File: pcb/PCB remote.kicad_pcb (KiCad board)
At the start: 2 copper layers, 58 x 84.9 mm, 11 parts, among them J1 Conn_01x01, J2 Conn_01x01, SW1 GREEN, SW2 RED, U1 RFM69HW, U2 SSD1306, U3 Joystick

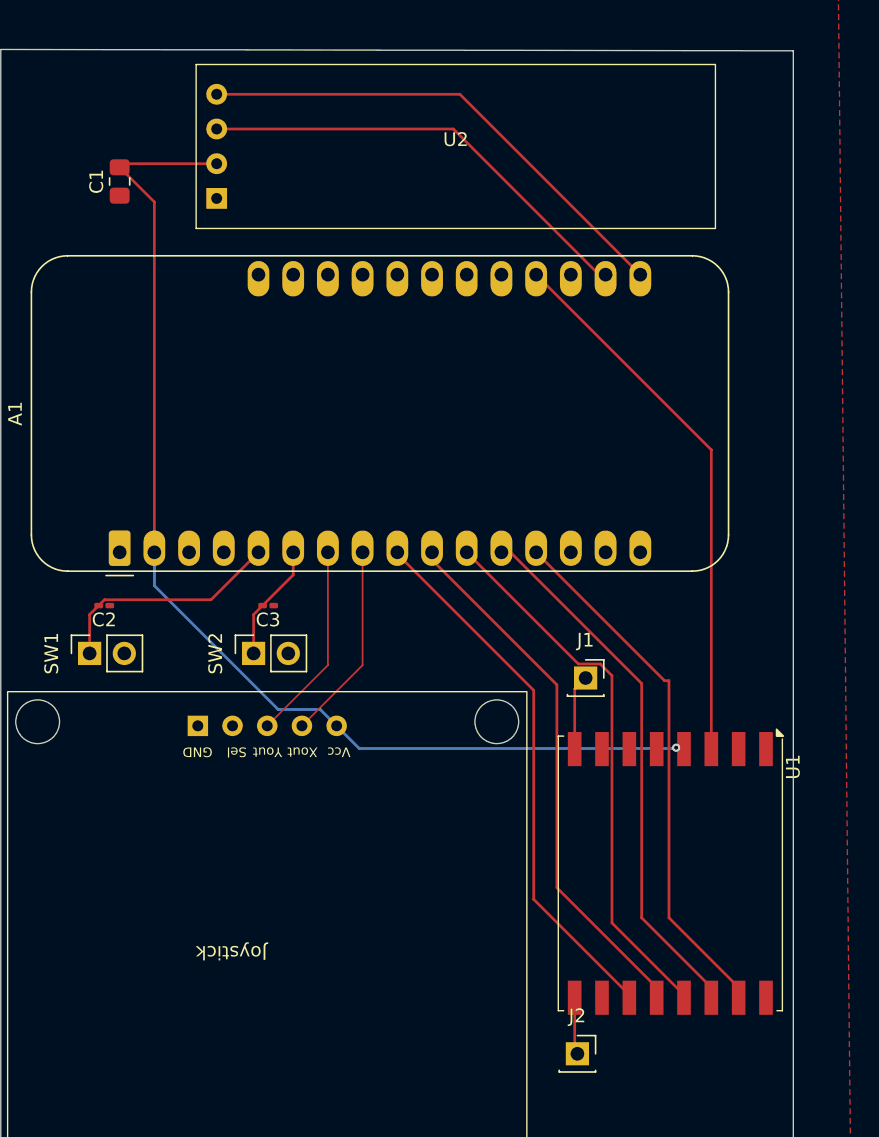
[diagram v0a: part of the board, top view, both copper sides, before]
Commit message: Update PCB design with latest changes
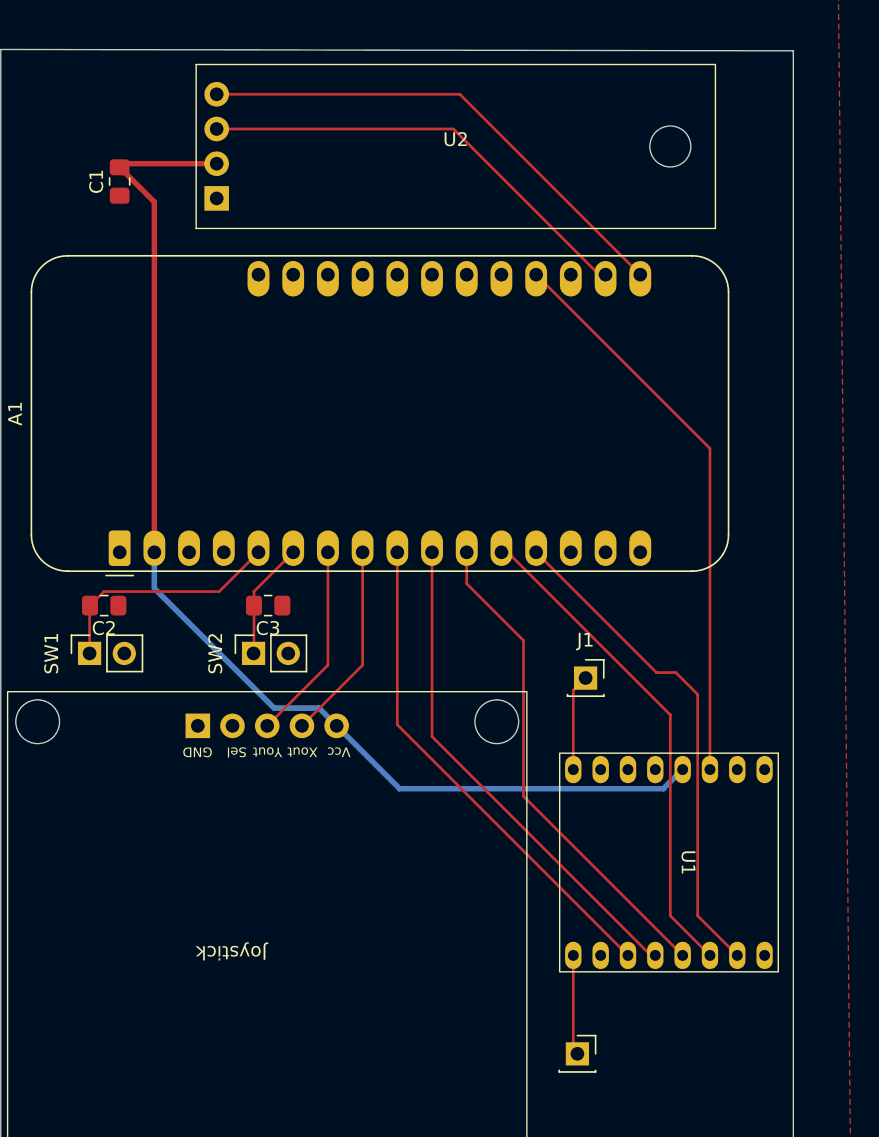
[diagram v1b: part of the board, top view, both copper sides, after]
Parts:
- C2, C3: footprint Capacitor_SMD:C_0201_0603Metric_Pad0.64x0.40mm_HandSolder -> Capacitor_SMD:C_0805_2012Metric_Pad1.18x1.45mm_HandSolder
- U1: footprint RF_Module:HOPERF_RFM69HW -> Remote-footprints:RFM69HCW(homemade)
- moved U1 0.81 mm to (170.7, 102.5)
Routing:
- net Net-(A1-SCK/D24): track 40.1 -> 36.0 mm
- net Net-(J2-Pin_1): track 4.18 -> 7.32 mm
- net Net-(A1-A4): track 39.6 -> 36.5 mm
- net Net-(A1-A5): track 39.4 -> 36.5 mm
- net Net-(A1-MOSI/D23): track 39.3 -> 36.8 mm
- net Net-(A1-MISO/D22): track 38.9 -> 36.4 mm
- net +3.3V: track 82.6 -> 84.4 mm, vias 1 -> 0
- net Net-(J1-Pin_1): track 5.53 -> 7.07 mm
- net Net-(A1-D6): track 40.0 -> 41.5 mm

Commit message: ny pcb og noget nyt code glete at gemme de andre dage men her er et push
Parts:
- added C4: 10uF, Capacitor_SMD:C_0805_2012Metric_Pad1.18x1.45mm_HandSolder, F.Cu at (141.2, 155.8)
- added J3: 02_Socket, Connector_JST:JST_PH_S2B-PH-K_1x02_P2.00mm_Horizontal, F.Cu at (136.1, 164.3)
- added J4: Conn_01x02_Socket, Connector_Wire:SolderWire-0.5sqmm_1x02_P4.8mm_D0.9mm_OD2.3mm, B.Cu at (166.5, 40.5)
- added Q1: PMV28XPEAR, Remote-footprints:Pmos, F.Cu at (142.7, 160.6)
- added Q2: BSS138, Remote-footprints:nmos, F.Cu at (149.3, 167.7)
- added R1: 220k, Resistor_SMD:R_0805_2012Metric_Pad1.20x1.40mm_HandSolder, F.Cu at (143.5, 167.5)
- added R2: 47k, Resistor_SMD:R_0603_1608Metric_Pad0.98x0.95mm_HandSolder, F.Cu at (150.9, 156.6)
- added S1: 100SP1T1B1M7QEH, Remote-footprints:100SP1T1B1M7QEH(redSwitch), B.Cu at (162.2, 165.5)
- added U4: HW373, Remote-footprints:HW373, F.Cu at (156.5, 131.0)
- C1: value 10u -> 10uF
- C2, C3: value 100n -> 100nF
- J1, J2, SW1, SW2, U2, U3: moved to B.Cu
- moved J2 64.6 mm to (162.1, 51.9)
- moved U2 49.1 mm to (155.7, 99.2)
- moved SW1 46.1 mm to (173.7, 79.3), turned to 180 degrees
- moved C2 40.6 mm to (169.9, 80.7), turned to 90 degrees
- moved A1 40.0 mm to (136.7, 40.2), turned to 0 degrees
- moved J1 38.5 mm to (175.7, 52.1)
- moved U1 37.8 mm to (168.9, 64.7), turned to 180 degrees
- moved C1 37.8 mm to (135.5, 90.2), turned to -90 degrees
- moved SW2 26.3 mm to (165.5, 79.8), turned to 180 degrees
- moved U3 24.6 mm to (156.3, 128.0), turned to 0 degrees
- moved C3 20.2 mm to (161.4, 81.0), turned to 90 degrees
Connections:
- A1 pad 19: unconnected-(A1-D5-Pad19) -> PWRControl
- A1 pad 28: unconnected-(A1-VBAT-Pad28) -> +BATT
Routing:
- net +BATT: track 0.00 -> 135.1 mm, vias 0 -> 1
- net PWRControl: track 0.00 -> 99.7 mm, vias 0 -> 2
- net Net-(A1-A2): track 14.5 -> 76.0 mm
- net Net-(A1-A3): track 14.5 -> 68.5 mm
- net +3.3V: track 84.4 -> 128.0 mm, vias 0 -> 1
- net Net-(J3-Pin_1): track 0.00 -> 41.8 mm
- net Net-(A1-A1): track 8.60 -> 43.1 mm, vias 0 -> 1
- net Net-(A1-DAC0/A0): track 17.5 -> 50.6 mm, vias 0 -> 1
- net Net-(S1-COM): track 0.00 -> 32.9 mm
- net Net-(J3-Pin_2): track 0.00 -> 32.8 mm
- net Net-(Q1-S): track 0.00 -> 22.7 mm
- net Net-(A1-D6): track 41.5 -> 19.9 mm
- net Net-(Q1-G): track 0.00 -> 15.8 mm
- net Net-(A1-MOSI/D23): track 36.8 -> 26.1 mm
- net Net-(A1-A4): track 36.5 -> 25.8 mm
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- added copper zone on B.Cu, net GND
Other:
- board outline removed
